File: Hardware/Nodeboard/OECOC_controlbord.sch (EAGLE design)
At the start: 3 parts, among them U1 ESP32-DEVKITC-32D

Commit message: hw update
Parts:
- added JP1: (no value), pinhead:PINHD-1X12
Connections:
- new net GND: U$1.GND.1, U1.GND1, U1.GND2, U1.GND3
- new net N$1: U$1.VCC.1, U1.EXT_5V
- new net N$2: U1.IO4
- new net N$3: U1.IO16
- new net N$4: U1.IO17
- new net N$5: U1.IO18
- new net SCL: U1.IO22
- new net SDA: U1.IO21

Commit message: update
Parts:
- removed JP1: (no value), pinhead:PINHD-1X12
- added U$3: PHOENIXCONTACT_PINSTRIP, Personal:PHOENIXCONTACT_PINSTRIP
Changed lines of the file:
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@@
 <part name="FRAME2" library="frames" library_urn="urn:adsk.eagle:library:229" deviceset="DINA3_L" device=""/>
 <part name="U$2" library="diy-modules" deviceset="TEMP-HUM-SENSOR-HTU21D" device=""/>
-<part name="JP1" library="pinhead" library_urn="urn:adsk.eagle:library:325" deviceset="PINHD-1X12" device="" package3d_urn="urn:adsk.eagle:package:22487/2"/>
 <part name="G1" library="IPEE-Lib" library_urn="urn:adsk.eagle:library:9142542" deviceset="GND" device=""/>
 <part name="G2" library="IPEE-Lib" library_urn="urn:adsk.eagle:library:9142542" deviceset="GND" device=""/>
 <part name="G3" library="IPEE-Lib" library_urn="urn:adsk.eagle:library:9142542" deviceset="GND" device=""/>
 <part name="G4" library="IPEE-Lib" library_urn="urn:adsk.eagle:library:9142542" deviceset="GND" device=""/>
+<part name="U$3" library="Personal" library_urn="urn:adsk.eagle:library:31195655" deviceset="PHOENIXCONTACT_PINSTRIP" device="" package3d_urn="urn:adsk.eagle:package:31348713/1"/>
 </parts>
 <sheets>
@@
 <attribute name="VALUE" x="43.18" y="210.82" size="1.778" layer="95"/>
 </instance>
-<instance part="JP1" gate="G$1" x="45.72" y="149.86" smashed="yes">
-<attribute name="NAME" x="39.37" y="165.735" size="1.778" layer="95"/>
-<attribute name="VALUE" x="39.37" y="129.54" size="1.778" layer="96"/>
-</instance>
 <instance part="G1" gate="G$1" x="256.54" y="198.12" smashed="yes" rot="R90">
 <attribute name="VALUE" x="259.715" y="196.215" size="1.778" layer="96" rot="R90"/>
@@
 <attribute name="VALUE" x="316.865" y="187.325" size="1.778" layer="96" rot="R270"/>
 </instance>
+<instance part="U$3" gate="G$1" x="116.84" y="170.18" smashed="yes"/>
 </instances>
 <busses>

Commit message: add external sensors and connectors
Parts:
- added IC1, IC2: DS2405, maxim:DS2405
- added S1, S2: REED-SWITCH-MK6-10, switch-reed:REED-SWITCH-MK6-10
- added U$4: CURRENT-SENSOR-ACS712, diy-modules:CURRENT-SENSOR-ACS712
- added U$5: TEMP-HUM-SENSOR-HTU21D, diy-modules:TEMP-HUM-SENSOR-HTU21D
- added U$6: PHOENIXCONTACT_PINSTRIP, Personal:PHOENIXCONTACT_PINSTRIP
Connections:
- new net +3V3: IC1.PIO, IC2.PIO, U$2.VIN, U$3.4, U$3.8, U$5.VIN, U$6.1
- new net +5V: U$1.VCC.1, U$4.VCC, U1.EXT_5V
- new net N$12: IC2.DATA, U$6.3
- new net N$13: IC1.DATA, U$6.4
- new net N$6: U$1.IN8, U1.IO15
- new net N$7: U$1.IN7, U1.IO2
- new net N$8: U$1.IN2, U1.IO19
- new net N$9: U$1.IN1, U1.IO23
- net GND: now also IC1.GND, IC2.GND, U$2.GND, U$3.3, U$3.7, U$4.GND, U$5.GND, U$6.2
- net N$1: now also U$4.OUT, U1.SENSOR_VP; no longer U$1.VCC.1, U1.EXT_5V
- net N$2: now also U$1.IN6
- net N$3: now also U$1.IN5
- net N$4: now also U$1.IN4
- net N$5: now also U$1.IN3
- net SCL: now also U$2.SCL, U$3.2, U$3.6, U$5.SCL
- net SDA: now also U$2.SDA, U$3.1, U$3.5, U$5.SDA
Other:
- moved on the sheet: U$2

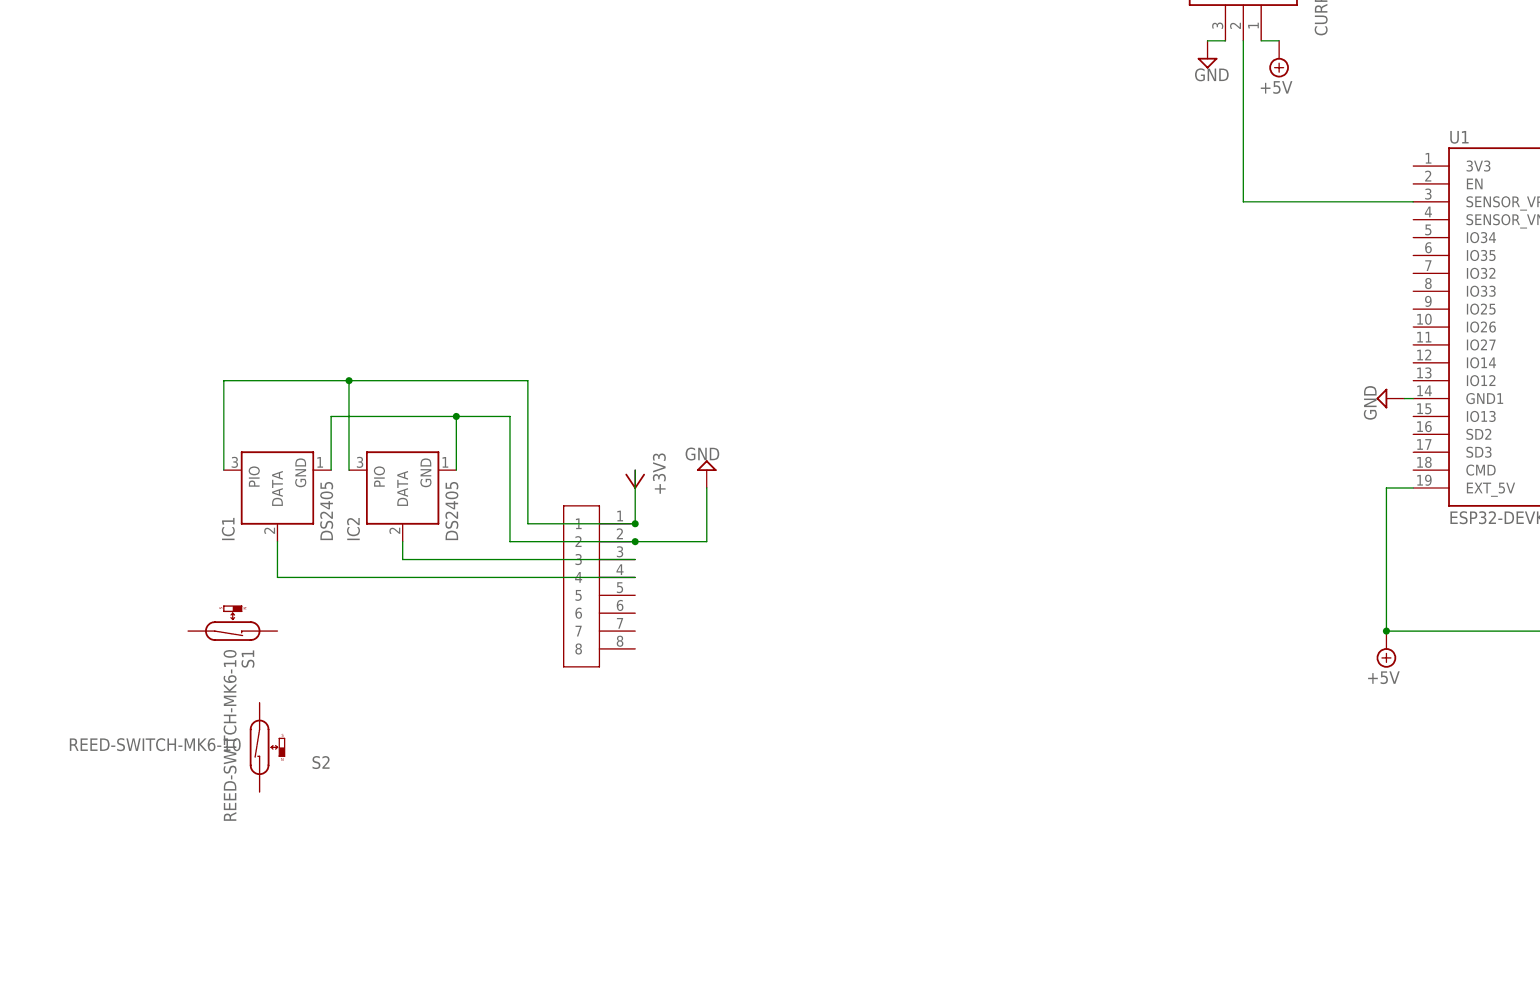
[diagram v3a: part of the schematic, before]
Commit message: add pin distribution
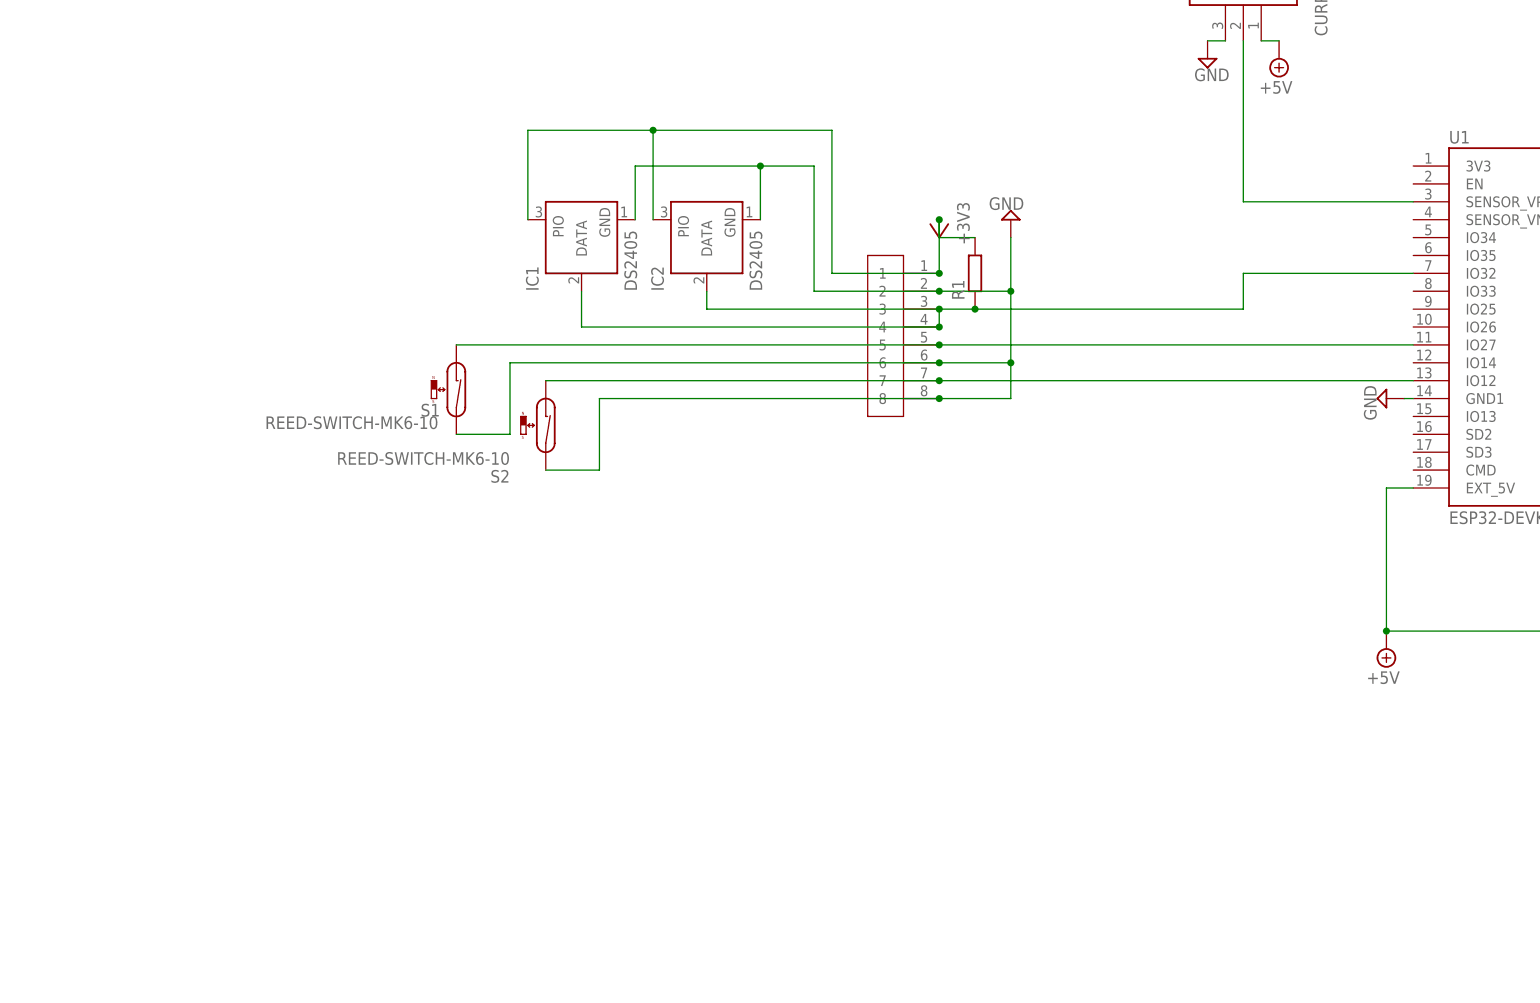
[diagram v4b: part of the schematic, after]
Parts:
- added R1: (no value), rcl:R-EU_0207/10
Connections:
- removed net N$12: IC2.DATA, U$6.3
- new net N$10: S1.1, U$6.5, U1.IO27
- new net N$14: S2.1, U$6.7, U1.IO12
- net +3V3: now also R1.2
- net GND: now also S1.2, S2.2, U$6.6, U$6.8
- net N$13: now also IC2.DATA, R1.1, U$6.3, U1.IO32
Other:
- moved on the sheet: IC1, IC2, S1, S2

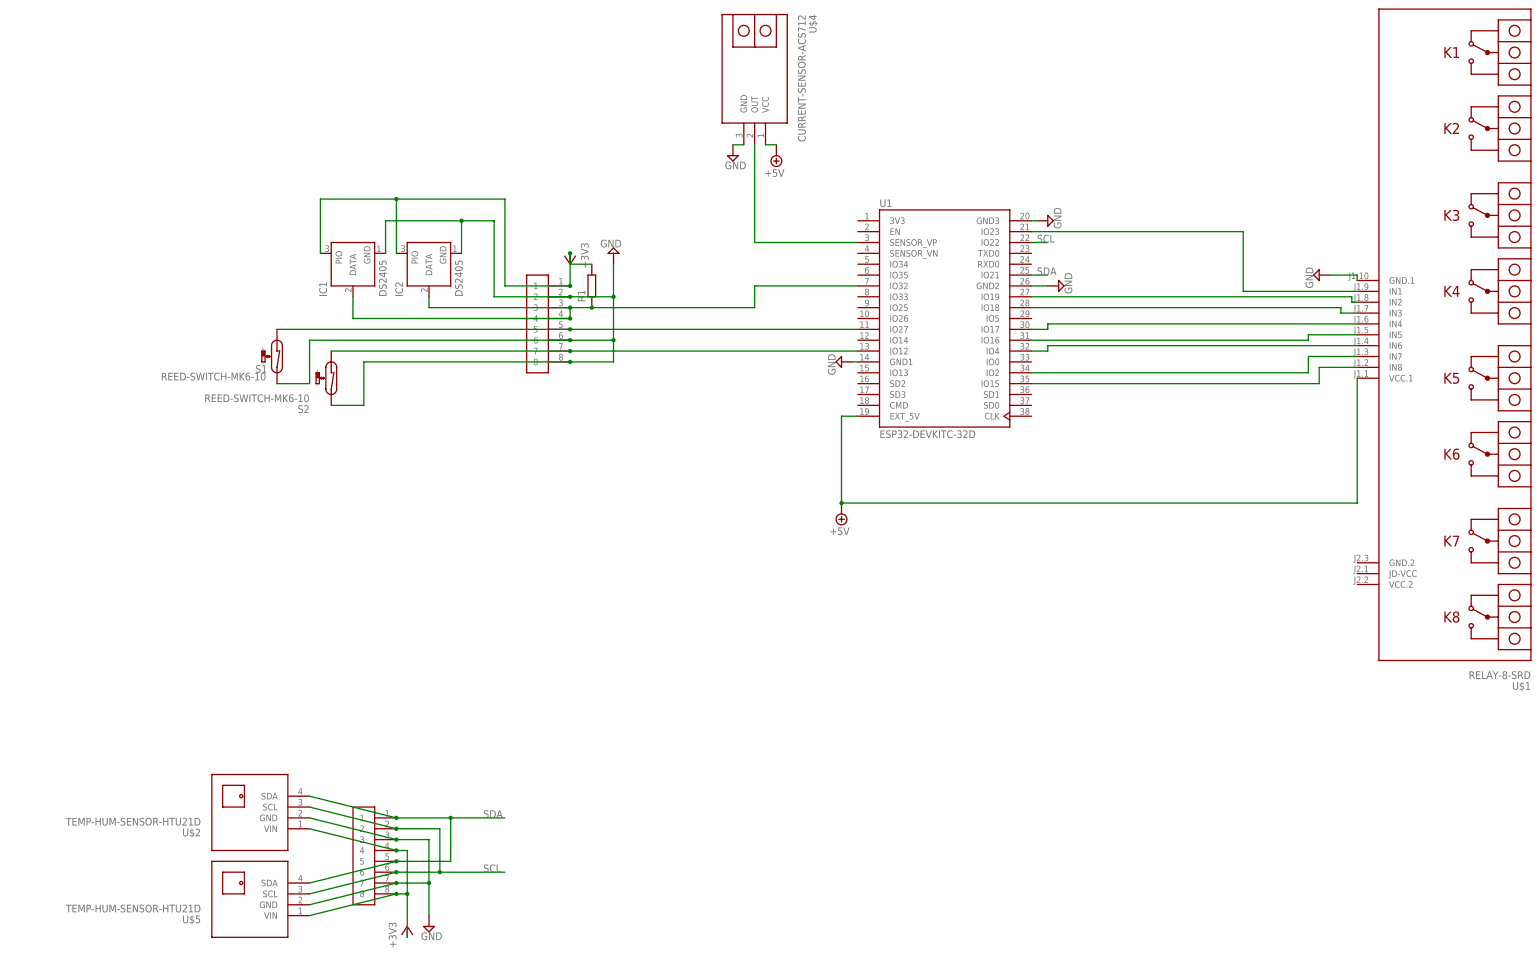
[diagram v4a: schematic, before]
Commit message: add buzzer
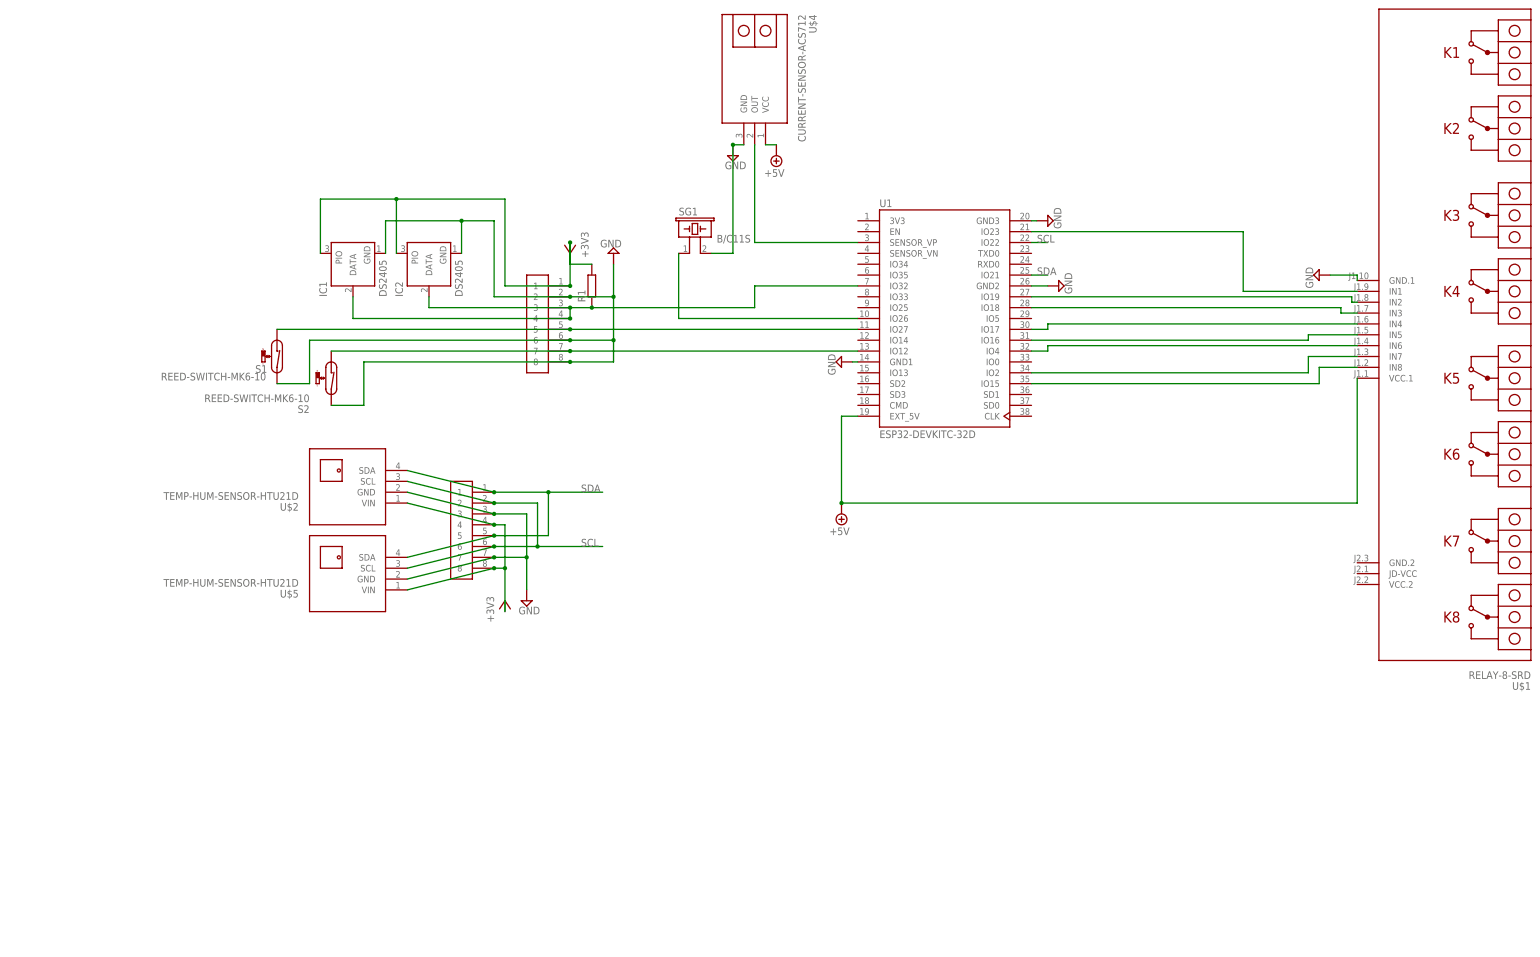
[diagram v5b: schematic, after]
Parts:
- added SG1: B/C11S, buzzer:B/C11S
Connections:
- new net N$11: SG1.1, U1.IO26
- net GND: now also SG1.2
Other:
- moved on the sheet: U$2, U$5
